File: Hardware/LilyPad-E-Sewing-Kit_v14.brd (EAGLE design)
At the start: 50.9 x 52.1 mm, 49 parts

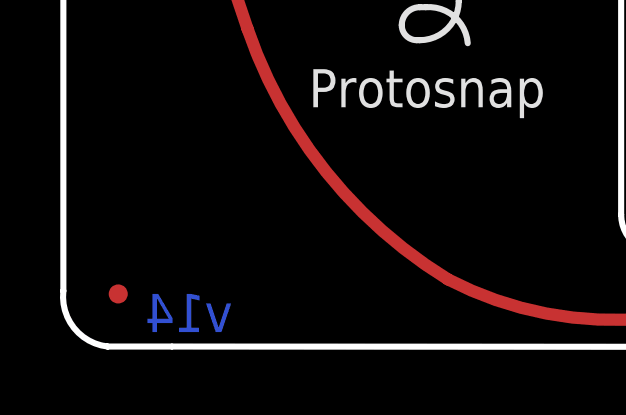
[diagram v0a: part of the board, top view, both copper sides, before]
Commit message: Silk update for consistency amongst the Lilypad product line.
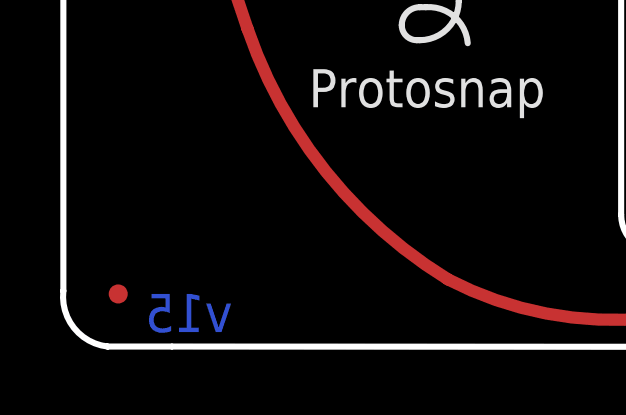
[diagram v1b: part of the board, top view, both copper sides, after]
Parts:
- added LOGO3: SFE_LOGO_NAME.1_INCH, SparkFun-Aesthetics:SFE_LOGO_NAME_.1
- U$4, U$7, U$8: device LilyPad-Wearables:LOGO-L-TINY -> LilyPad-Wearables:LOGO-L
- moved U$7 9.30 mm to (33.6, 9.33)
- moved U$8 9.07 mm to (24.5, 9.20)
- moved U$6 1.13 mm to (46.0, 35.5), turned to 90 degrees
- moved U$5 0.99 mm to (36.3, 35.5), turned to 90 degrees
- moved U$4 0.49 mm to (42.5, 9.33)
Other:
- board text added: "Button"
- board text added: "Switch"
- board text added: "White"
- board text added: "sparkfun.com/esewing"
- board text added: "v15"
- board text removed: "v14"
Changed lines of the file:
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@@
 <?xml version="1.0" encoding="utf-8"?>
 <!DOCTYPE eagle SYSTEM "eagle.dtd">
-<eagle version="7.5.0">
+<eagle version="7.7.0">
 <drawing>
 <settings>
@@
 <layer number="14" name="Route14" color="1" fill="6" visible="no" active="no"/>
 <layer number="15" name="Route15" color="4" fill="6" visible="no" active="no"/>
-<layer number="16" name="Bottom" color="1" fill="1" visible="no" active="yes"/>
-<layer number="17" name="Pads" color="2" fill="1" visible="no" active="yes"/>
-<layer number="18" name="Vias" color="2" fill="1" visible="no" active="yes"/>
+<layer number="16" name="Bottom" color="1" fill="1" visible="yes" active="yes"/>
+<layer number="17" name="Pads" color="2" fill="1" visible="yes" active="yes"/>
+<layer number="18" name="Vias" color="2" fill="1" visible="yes" active="yes"/>
 <layer number="19" name="Unrouted" color="6" fill="1" visible="yes" active="yes"/>
-<layer number="20" name="Dimension" color="15" fill="1" visible="no" active="yes"/>
-<layer number="21" name="tPlace" color="16" fill="1" visible="no" active="yes"/>
+<layer number="20" name="Dimension" color="15" fill="1" visible="yes" active="yes"/>
+<layer number="21" name="tPlace" color="16" fill="1" visible="yes" active="yes"/>
 <layer number="22" name="bPlace" color="14" fill="1" visible="no" active="yes"/>
-<layer number="23" name="tOrigins" color="15" fill="1" visible="no" active="yes"/>
+<layer number="23" name="tOrigins" color="15" fill="1" visible="yes" active="yes"/>
 <layer number="24" name="bOrigins" color="15" fill="1" visible="no" active="yes"/>
-<layer number="25" name="tNames" color="7" fill="1" visible="no" active="yes"/>
+<layer number="25" name="tNames" color="7" fill="1" visible="yes" active="yes"/>
 <layer number="26" name="bNames" color="7" fill="1" visible="no" active="yes"/>
 <layer number="27" name="tValues" color="7" fill="1" visible="no" active="yes"/>
@@
 <layer number="112" name="tSilk" color="7" fill="1" visible="no" active="yes"/>
 <layer number="113" name="IDFDebug" color="4" fill="1" visible="no" active="yes"/>
+<layer number="114" name="Badge_Outline" color="7" fill="1" visible="no" active="yes"/>
+<layer number="115" name="ReferenceISLANDS" color="7" fill="1" visible="no" active="yes"/>
 <layer number="116" name="Patch_BOT" color="9" fill="4" visible="no" active="yes"/>
 <layer number="118" name="Rect_Pads" color="7" fill="1" visible="no" active="yes"/>
@@
 <text x="31.1658" y="6.52018125" size="1.778" layer="21" font="vector" ratio="15">-</text>
 <text x="40.0456375" y="6.49478125" size="1.778" layer="21" font="vector" ratio="15">-</text>
-<text x="26.56331875" y="11.346184375" size="1.778" layer="22" font="vector" ratio="15" rot="MR0">+</text>
-<text x="23.301959375" y="6.44398125" size="1.778" layer="22" font="vector" ratio="15" rot="MR0">-</text>
-<text x="35.722559375" y="11.356340625" size="1.778" layer="22" font="vector" ratio="15" rot="MR0">+</text>
-<text x="44.79798125" y="11.353803125" size="1.778" layer="22" font="vector" ratio="15" rot="MR0">+</text>
-<text x="41.33341875" y="6.497321875" size="1.778" layer="22" font="vector" ratio="15" rot="MR0">-</text>
-<text x="32.435803125" y="6.52018125" size="1.778" layer="22" font="vector" ratio="15" rot="MR0">-</text>
+<text x="44.79798125" y="12.369803125" size="1.524" layer="22" font="vector" ratio="15" rot="MR0">+</text>
+<text x="41.20641875" y="6.497321875" size="1.27" layer="22" font="vector" ratio="15" rot="MR0">-</text>
 <hole x="4.074159375" y="23.281640625" drill="0.508"/>
 <hole x="5.877559375" y="21.605240625" drill="0.508"/>
@@
 <text x="-37.335459375" y="57.0484" size="1.778" layer="47" font="vector" ratio="15">All Units Inches</text>
 <text x="66.94678125" y="37.640259375" size="1.778" layer="51" font="vector" ratio="15">Board Thickness: 0.032"</text>
-<text x="5.588" y="0.381" size="1.27" layer="16" font="vector" ratio="15" rot="MR0">v14</text>
+<text x="5.588" y="0.381" size="1.27" layer="16" font="vector" ratio="15" rot="MR0">v15</text>
 <text x="33.6296" y="41.021" size="0.8128" layer="21" font="vector" ratio="15" rot="R270">ON</text>
 <text x="34.3662" y="30.7594" size="0.8128" layer="21" font="vector" ratio="15" rot="R90">OFF</text>
@@
 <dimension x1="5.08" y1="44.831" x2="26.0858" y2="44.831" x3="15.5829" y3="56.25338125" textsize="1.778" textratio="15" layer="47" unit="inch"/>
 <dimension x1="5.08" y1="44.831" x2="7.0358" y2="24.003" x3="-6.147421875" y3="33.270890625" textsize="1.778" textratio="15" layer="47" unit="inch"/>
+<text x="49.022" y="33.02" size="1.27" layer="22" font="vector" ratio="15" rot="MR90">Button</text>
+<text x="38.862" y="32.893" size="1.27" layer="22" font="vector" ratio="15" rot="MR90">Switch</text>
+<text x="44.196" y="11.303" size="1.016" layer="22" font="vector" ratio="15" rot="MR0">White</text>
+<text x="35.90798125" y="12.369803125" size="1.524" layer="22" font="vector" ratio="15" rot="MR0">+</text>
+<text x="32.31641875" y="6.497321875" size="1.27" layer="22" font="vector" ratio="15" rot="MR0">-</text>
+<text x="35.306" y="11.303" size="1.016" layer="22" font="vector" ratio="15" rot="MR0">White</text>
+<text x="26.76398125" y="12.242803125" size="1.524" layer="22" font="vector" ratio="15" rot="MR0">+</text>
+<text x="23.17241875" y="6.370321875" size="1.27" layer="22" font="vector" ratio="15" rot="MR0">-</text>
+<text x="26.162" y="11.176" size="1.016" layer="22" font="vector" ratio="15" rot="MR0">White</text>
+<text x="49.53" y="17.78" size="1.524" layer="22" font="vector" ratio="15" rot="MR0">sparkfun.com/esewing</text>
 </plain>
 <attributes>
@@
 <element name="U$2" library="LilyPad-Wearables" package="LOGO-LILYPAD" value="" x="12.319" y="12.6746"/>
 <element name="U$3" library="LilyPad-Wearables" package="LOGO-LILYPAD" value="" x="15.2908" y="36.4998" rot="MR0"/>
-<element name="U$4" library="LilyPad-Wearables" package="LOGO-L-TINY" value="" x="42.458640625" y="9.80948125" rot="MR0"/>
-<element name="U$7" library="LilyPad-Wearables" package="LOGO-L-TINY" value="" x="24.33828125" y="9.865359375" rot="MR0"/>
-<element name="U$8" library="LilyPad-Wearables" package="LOGO-L-TINY" value="" x="33.51784375" y="9.923784375" rot="MR0"/>
-<element name="U$5" library="LilyPad-Wearables" package="LOGO-L" value="" x="36.890959375" y="36.25088125" rot="MR0"/>
-<element name="U$6" library="LilyPad-Wearables" package="LOGO-L" value="" x="47.08144375" y="35.86988125" rot="MR0"/>
+<element name="U$5" library="LilyPad-Wearables" package="LOGO-L" value="" x="36.25088125" y="35.499040625" rot="MR90"/>
+<element name="U$6" library="LilyPad-Wearables" package="LOGO-L" value="" x="46.02988125" y="35.46855625" rot="MR90"/>
 <element name="LOGO1" library="SparkFun-Aesthetics" package="SFE_LOGO_FLAME_.1" value="SFE_LOGO_FLAME.1_INCH" x="11.049" y="46.4058" rot="MR0"/>
 <element name="LOGO2" library="SparkFun-Aesthetics" package="OSHW-LOGO-S" value="OSHW-LOGOS" x="21.336" y="47.8282" rot="MR0"/>
 <element name="FD1" library="SparkFun-Aesthetics" package="MICRO-FIDUCIAL" value="FIDUCIALUFIDUCIAL" x="48.768" y="49.911"/>
 <element name="FD2" library="SparkFun-Aesthetics" package="MICRO-FIDUCIAL" value="FIDUCIALUFIDUCIAL" x="1.778" y="1.651"/>
+<element name="U$4" library="LilyPad-Wearables" package="LOGO-L" value="" x="42.50944375" y="9.32688125" rot="MR0"/>
+<element name="U$7" library="LilyPad-Wearables" package="LOGO-L" value="" x="33.61944375" y="9.32688125" rot="MR0"/>
+<element name="U$8" library="LilyPad-Wearables" package="LOGO-L" value="" x="24.47544375" y="9.19988125" rot="MR0"/>
+<element name="LOGO3" library="SparkFun-Aesthetics" package="SFE_LOGO_NAME_.1" value="SFE_LOGO_NAME.1_INCH" x="15.24" y="2.54" rot="MR0"/>
 </elements>
 <signals>

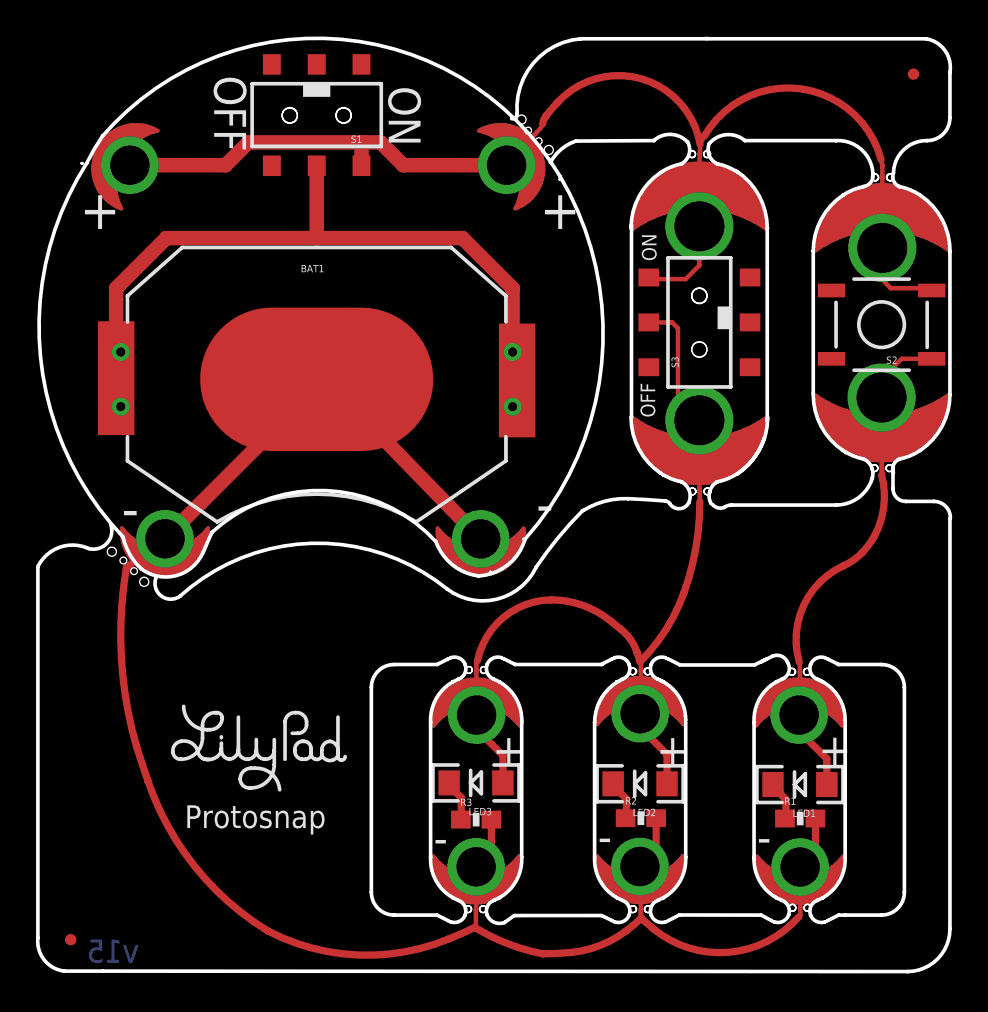
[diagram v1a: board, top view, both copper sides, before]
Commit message: Updated schematic
Special Ordering Instructions, two more fiducials, dashed lines to
dilineate parts along with labels amongst other minor changes.
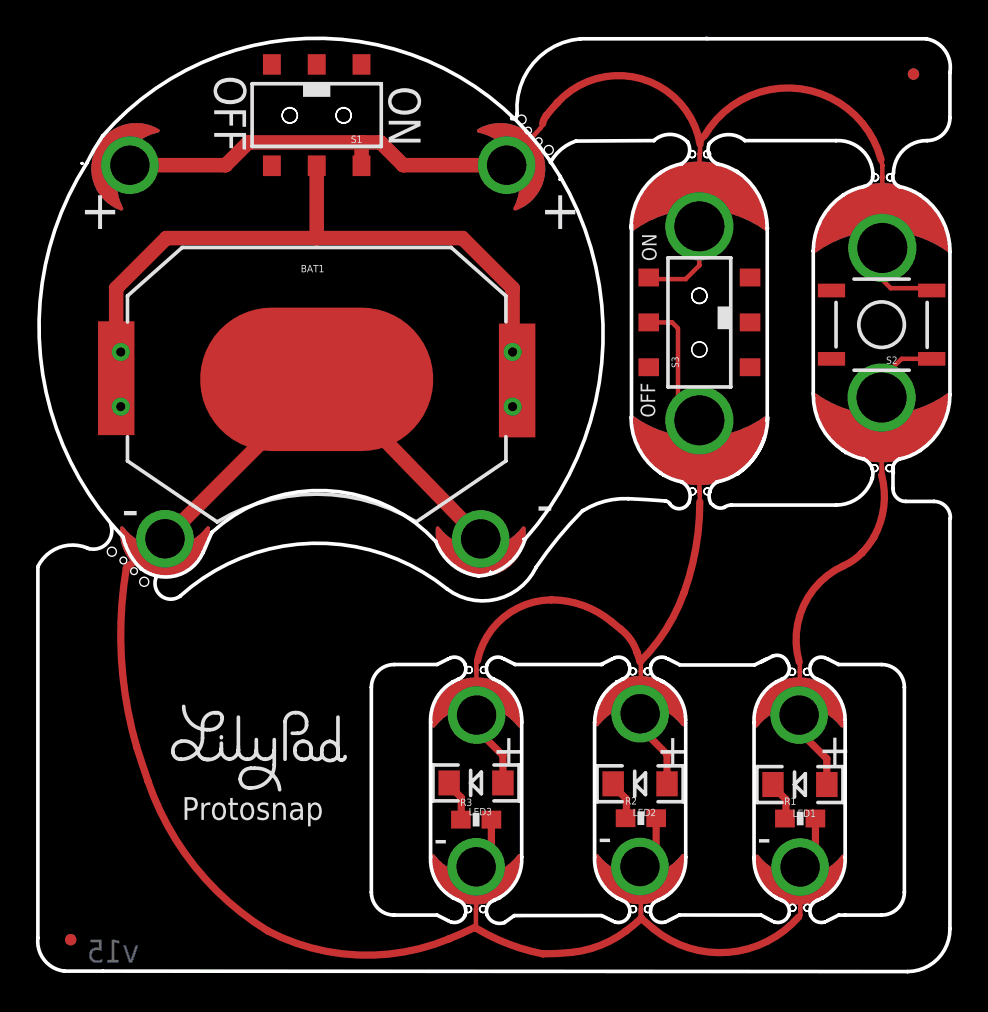
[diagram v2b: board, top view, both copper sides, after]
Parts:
- added FD3, FD4: FIDUCIALUFIDUCIAL, SparkFun-Aesthetics:MICRO-FIDUCIAL
- added U$9: SPECIAL_INSTRUCTIONS-ORDERING, SparkFun-Aesthetics:ORDERING_INSTRUCTIONS
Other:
- board text added: "Elias Santistevan"
- board text removed: "M. West"
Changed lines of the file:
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@@
 <setting verticaltext="up"/>
 </settings>
-<grid distance="0.05" unitdist="inch" unit="inch" style="lines" multiple="1" display="yes" altdistance="0.005" altunitdist="inch" altunit="inch"/>
+<grid distance="1" unitdist="mil" unit="mil" style="lines" multiple="1" display="yes" altdistance="0.005" altunitdist="inch" altunit="inch"/>
 <layers>
 <layer number="1" name="Top" color="4" fill="1" visible="yes" active="yes"/>
@@
 <layer number="155" name="FabDoc3" color="7" fill="1" visible="no" active="yes"/>
 <layer number="199" name="Contour" color="7" fill="1" visible="no" active="yes"/>
-<layer number="200" name="200bmp" color="1" fill="10" visible="no" active="no"/>
+<layer number="200" name="200bmp" color="1" fill="10" visible="no" active="yes"/>
 <layer number="201" name="201bmp" color="2" fill="1" visible="no" active="no"/>
 <layer number="202" name="202bmp" color="3" fill="1" visible="no" active="no"/>
@@
 <hole x="28.432759375" y="45.679359375" drill="0.508"/>
 <text x="31.60268125" y="-18.90521875" size="1.778" layer="51" font="vector" ratio="15">L. Buechley, N. Seidle, P. Lewis, T. Klopfenstein</text>
-<text x="31.711903125" y="-22.6187" size="1.778" layer="51" font="vector" ratio="15">M. West</text>
 <text x="-37.335459375" y="57.0484" size="1.778" layer="47" font="vector" ratio="15">All Units Inches</text>
-<text x="66.94678125" y="37.640259375" size="1.778" layer="51" font="vector" ratio="15">Board Thickness: 0.032"</text>
+<text x="-8.87221875" y="-40.464740625" size="1.778" layer="51" font="vector" ratio="15">Board Thickness: 0.032"</text>
 <text x="5.588" y="0.381" size="1.27" layer="16" font="vector" ratio="15" rot="MR0">v15</text>
 <text x="33.6296" y="41.021" size="0.8128" layer="21" font="vector" ratio="15" rot="R270">ON</text>
@@
 <text x="26.162" y="27.051" size="2.1844" layer="22" font="vector" ratio="15" rot="MR180">-</text>
 <text x="3.048" y="26.797" size="2.1844" layer="22" font="vector" ratio="15" rot="MR180">-</text>
-<text x="8.128" y="7.874" size="1.27" layer="21" font="vector" ratio="15" rot="SR0">Protosnap</text>
+<text x="7.9756" y="8.3312" size="1.27" layer="21" font="vector" ratio="15" rot="SR0">Protosnap</text>
 <rectangle x1="37.846" y1="35.687" x2="38.608" y2="36.957" layer="21"/>
 <rectangle x1="14.732" y1="48.641" x2="16.256" y2="49.403" layer="21"/>
@@
 <wire x1="33.5407" y1="2.8448" x2="35.00628125" y2="1.77038125" width="0.4572" layer="29"/>
 <wire x1="33.550859375" y1="2.829559375" x2="33.55848125" y2="3.710940625" width="0.4572" layer="29"/>
-<text x="66.215259375" y="31.69411875" size="1.778" layer="51" font="vector" ratio="15">Purple Solder Mask</text>
+<text x="-8.841740625" y="-43.23588125" size="1.778" layer="51" font="vector" ratio="15">Purple Solder Mask</text>
 <wire x1="24.462740625" y1="17.272" x2="24.406859375" y2="16.393159375" width="0.4572" layer="29"/>
 <wire x1="5.1816" y1="22.646640625" x2="4.9149" y2="22.400259375" width="0.4572" layer="29"/>
@@
 <text x="23.17241875" y="6.370321875" size="1.27" layer="22" font="vector" ratio="15" rot="MR0">-</text>
 <text x="26.162" y="11.176" size="1.016" layer="22" font="vector" ratio="15" rot="MR0">White</text>
-<text x="49.53" y="17.78" size="1.524" layer="22" font="vector" ratio="15" rot="MR0">sparkfun.com/esewing</text>
+<text x="45.72" y="17.78" size="1.524" layer="22" font="vector" ratio="15" rot="MR0">sparkfun.com/esewing</text>
+<text x="31.75" y="-22.86" size="1.778" layer="51" font="vector" ratio="15">Elias Santistevan</text>
 </plain>
 <attributes>
@@
 <element name="U$8" library="LilyPad-Wearables" package="LOGO-L" value="" x="24.47544375" y="9.19988125" rot="MR0"/>
 <element name="LOGO3" library="SparkFun-Aesthetics" package="SFE_LOGO_NAME_.1" value="SFE_LOGO_NAME.1_INCH" x="15.24" y="2.54" rot="MR0"/>
+<element name="U$9" library="SparkFun-Aesthetics" package="ORDERING_INSTRUCTIONS" value="SPECIAL_INSTRUCTIONS-ORDERING" x="-10.16" y="-26.67"/>
+<element name="FD3" library="SparkFun-Aesthetics" package="MICRO-FIDUCIAL" value="FIDUCIALUFIDUCIAL" x="48.768" y="49.911" rot="MR0"/>
+<element name="FD4" library="SparkFun-Aesthetics" package="MICRO-FIDUCIAL" value="FIDUCIALUFIDUCIAL" x="1.778" y="1.651" rot="MR0"/>
 </elements>
 <signals>

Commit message: Final text object put into place
"E-Sewing Protosnap" was added as silk according to dimension outlines
specified in the Lilypad document provided by Lilypad Coordinator.
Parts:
- LOGO3: value SFE_LOGO_NAME.1_INCH -> SFE_LOGO_NAME_FLAME.1_INCH; device SparkFun-Aesthetics:SFE_LOGO_NAME_.1 -> SparkFun-Aesthetics:SFE_LOGO_NAME_FLAME_.1
- moved U$2 2.54 mm to (12.3, 10.1)
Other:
- board text removed: "Protosnap"
